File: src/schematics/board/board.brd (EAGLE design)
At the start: 50.8 x 35.6 mm, 26 parts, among them P1 PN61729-S, Q1 12MHz, U1 MCP17003302E/TO, U2 PIC18LF14K50-E-P

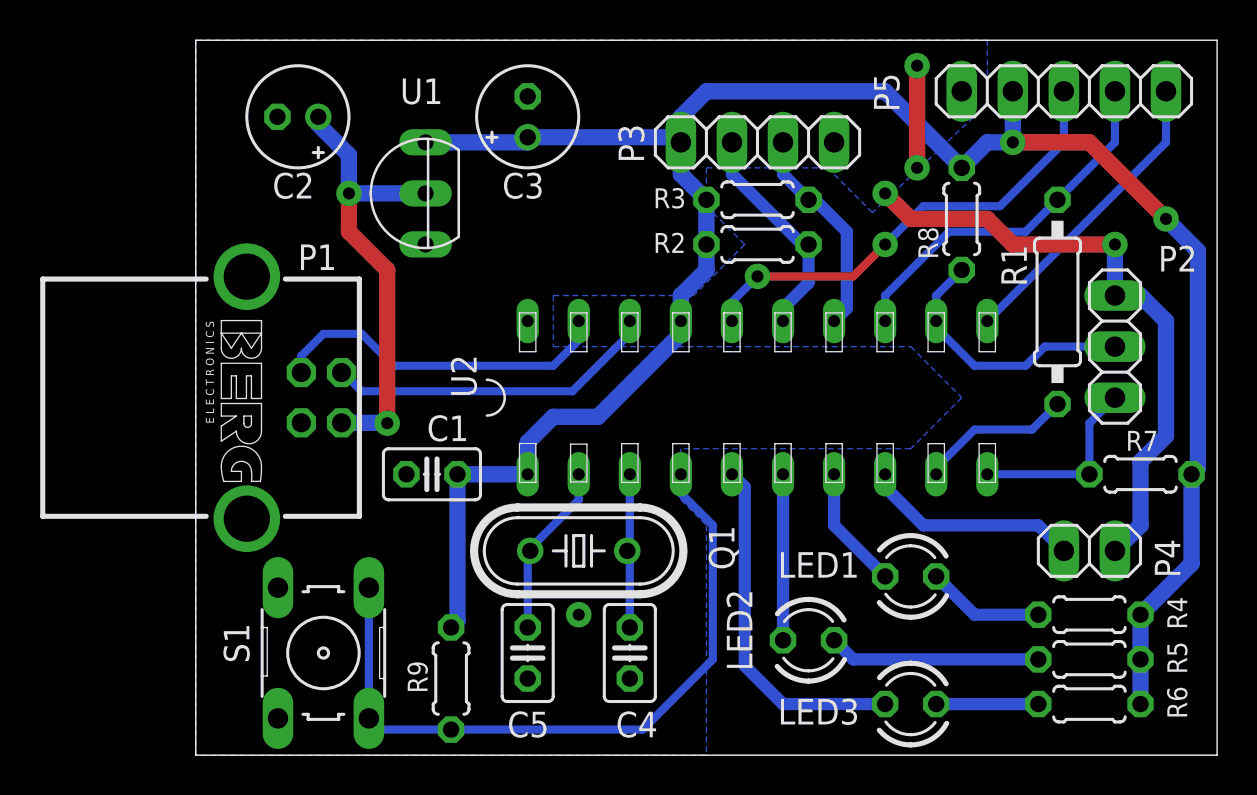
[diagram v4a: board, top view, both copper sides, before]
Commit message: Fixed PCB libraries
Some components in the extended Microxhip library had wrong dual-in-line
package drawings.

The libraries were renamed as "local" instead of "extended".

Minor fixes in both schematics and PCBs.

Andrea Zoppi
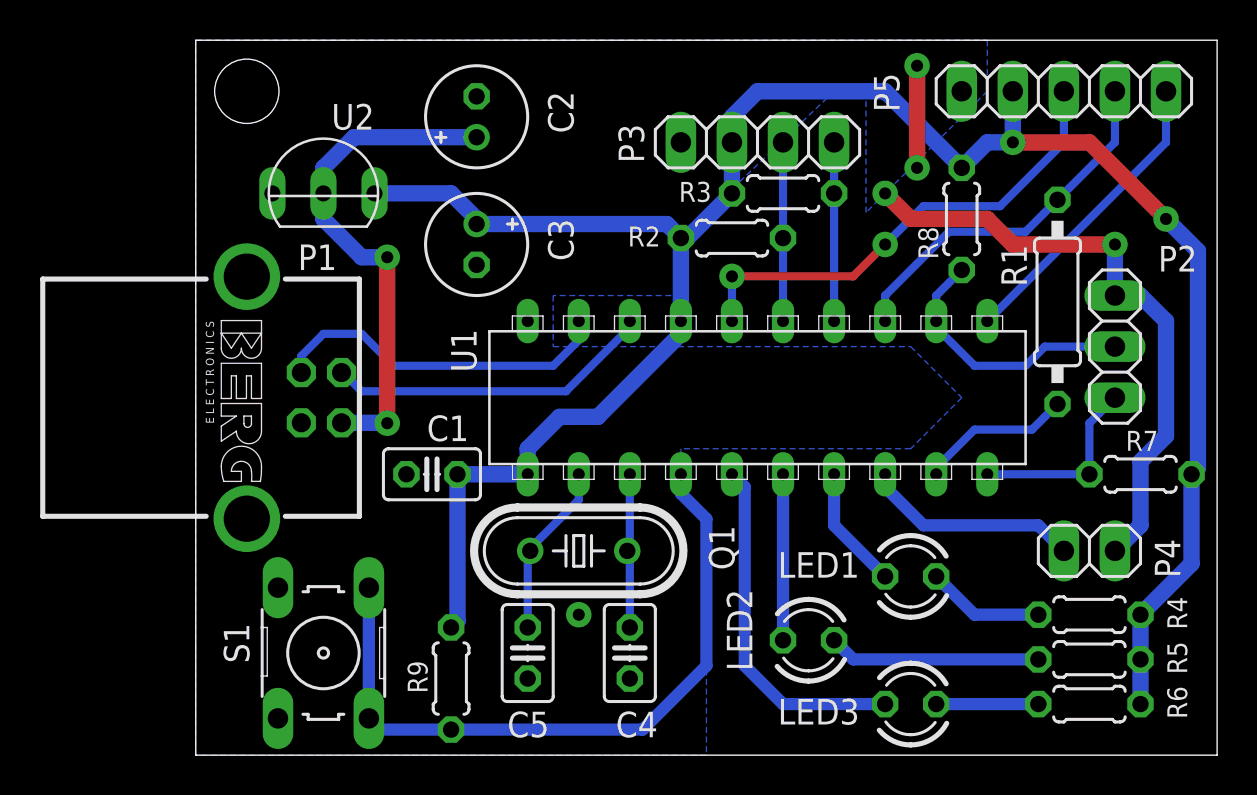
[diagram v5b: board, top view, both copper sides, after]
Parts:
- U1: value MCP17003302E/TO -> PIC18F14K50-E-P; device microchip_extended:TO-92 -> microchip_local:DIP-20
- U2: value PIC18LF14K50-E-P -> MCP17003302E/TO; device microchip_extended:PIC18F14K50-E/P -> microchip_local:TO-92
- moved U2 22.7 mm to (6.35, 27.9), turned to 0 degrees
- moved U1 19.4 mm to (27.9, 17.8)
- moved C2 8.89 mm to (14.0, 31.8), turned to 90 degrees
- moved C3 6.84 mm to (14.0, 25.4), turned to 270 degrees
- moved R2 1.31 mm to (26.7, 25.7)
- moved R3 1.31 mm to (29.2, 27.9)
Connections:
- removed net ENC_A: P3.2, R2.1, U2.15
- removed net ENC_B: P3.3, R3.1, U2.14
- new net QA: P3.3, R2.1, U1.15
- new net QB: P3.4, R3.1, U1.14
- net +3V3: now also P3.2, U1.1, U1.17, U2.OUT; no longer P3.1, U1.OUT, U2.1, U2.17
- net +5V: now also U2.IN; no longer U1.IN
- net AUXIN: now also U1.8; no longer U2.8
- net D+: now also U1.19; no longer U2.19
- net D-: now also U1.18; no longer U2.18
- net GND: now also P3.1, U1.20, U2.GND; no longer P3.4, U1.GND, U2.20
- net GREEN: now also U1.7; no longer U2.7
- net MOSI: now also U1.9; no longer U2.9
- net MOTION: now also U1.16; no longer U2.16
- net N$2: now also U1.3; no longer U2.3
- net N$3: now also U1.2; no longer U2.2
- net RED: now also U1.5; no longer U2.5
- net RST: now also U1.4; no longer U2.4
- net RX: now also U1.12; no longer U2.12
- net SCLK: now also U1.11; no longer U2.11
- net SDIO: now also U1.13; no longer U2.13
- net TX: now also U1.10; no longer U2.10
- net YELLOW: now also U1.6; no longer U2.6
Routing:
- net ENC_A: track 11.2 -> 0.00 mm
- net ENC_B: track 10.7 -> 0.00 mm
- net QB: track 0.00 -> 8.89 mm
- net QA: track 0.00 -> 8.89 mm
- net +5V: track 22.8 -> 25.3 mm
- net +3V3: track 104.4 -> 105.2 mm
- net MOTION: track 23.3 -> 24.0 mm

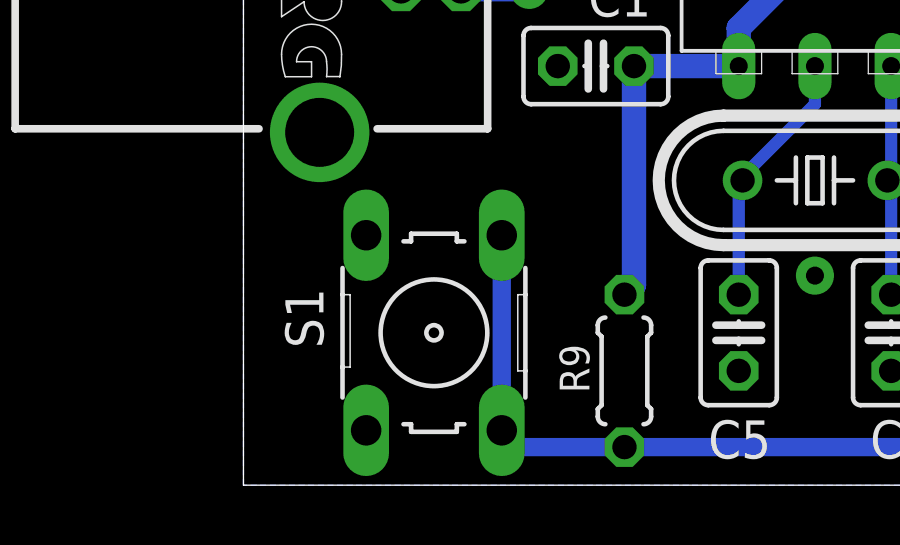
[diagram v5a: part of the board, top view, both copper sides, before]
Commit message: WIP: Improving debug messages
The debug console is being improved to reduce the footprint (by using
preprocessor definitions) and the overall performance.

Andrea Zoppi
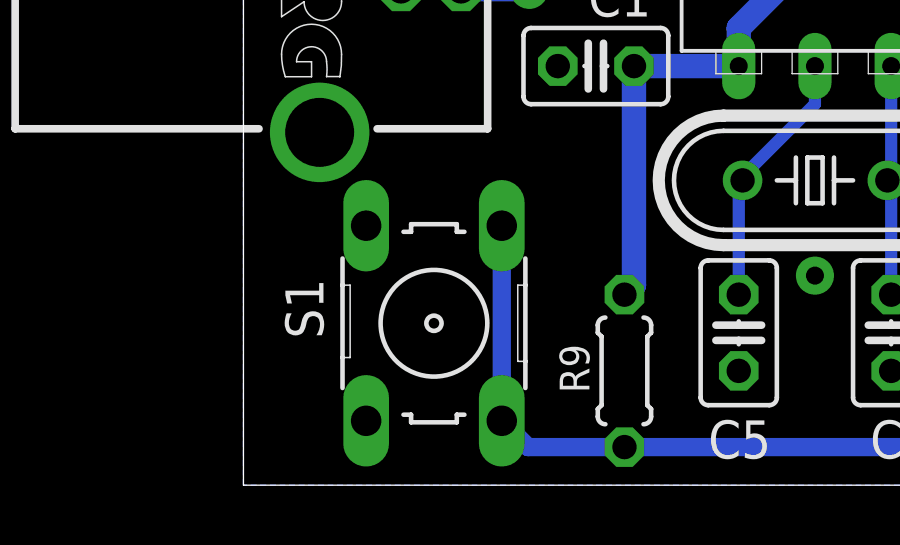
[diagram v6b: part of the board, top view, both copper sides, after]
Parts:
- U1: device microchip_local:DIP-20 -> microchip_local:DIL20
- moved S1 0.32 mm to (6.35, 5.40)
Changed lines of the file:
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@@
 <attribute name="NAME" x="25.527" y="11.43" size="1.27" layer="25" ratio="10" rot="R270"/>
 </element>
-<element name="S1" library="switch-omron" package="B3F-10XX" value="" x="6.35" y="5.08" smashed="yes" rot="R270">
-<attribute name="OC_NEWARK" value="36M3542" x="-26.67" y="-13.97" size="1.778" layer="27" rot="R270" display="off"/>
-<attribute name="MPN" value="B3F-1000" x="-26.67" y="-13.97" size="1.778" layer="27" rot="R270" display="off"/>
-<attribute name="MF" value="" x="-26.67" y="-13.97" size="1.778" layer="27" rot="R270" display="off"/>
-<attribute name="OC_FARNELL" value="176432" x="-26.67" y="-13.97" size="1.778" layer="27" rot="R270" display="off"/>
-<attribute name="NAME" x="2.667" y="4.572" size="1.27" layer="25" ratio="10" rot="R90"/>
-<attribute name="VALUE" x="1.27" y="8.128" size="1.27" layer="27" ratio="10" rot="R270"/>
+<element name="S1" library="switch-omron" package="B3F-10XX" value="" x="6.35" y="5.3975" smashed="yes" rot="R270">
+<attribute name="OC_NEWARK" value="36M3542" x="-26.67" y="-13.6525" size="1.778" layer="27" rot="R270" display="off"/>
+<attribute name="MPN" value="B3F-1000" x="-26.67" y="-13.6525" size="1.778" layer="27" rot="R270" display="off"/>
+<attribute name="MF" value="" x="-26.67" y="-13.6525" size="1.778" layer="27" rot="R270" display="off"/>
+<attribute name="OC_FARNELL" value="176432" x="-26.67" y="-13.6525" size="1.778" layer="27" rot="R270" display="off"/>
+<attribute name="NAME" x="2.667" y="4.8895" size="1.27" layer="25" ratio="10" rot="R90"/>
+<attribute name="VALUE" x="1.27" y="8.4455" size="1.27" layer="27" ratio="10" rot="R270"/>
 </element>
 <element name="P2" library="pinhead" package="1X03" value="" x="45.72" y="20.32" smashed="yes" rot="R90">
@@
 <attribute name="NAME" x="11.5316" y="3.0734" size="0.9906" layer="25" ratio="10" rot="R90"/>
 </element>
-<element name="U1" library="microchip_local" package="DIP-20" value="PIC18F14K50-E-P" x="27.94" y="17.78" smashed="yes" rot="R90">
+<element name="U1" library="microchip_local" package="DIL20" value="PIC18F14K50-E-P" x="27.94" y="17.78" smashed="yes" rot="R90">
 <attribute name="NAME" x="13.97" y="19.05" size="1.27" layer="25" rot="R90"/>
 </element>
@@
 <contactref element="U1" pad="4"/>
 <wire x1="24.13" y1="13.0175" x2="24.13" y2="13.97" width="0.6096" layer="16"/>
-<wire x1="8.6106" y1="1.8288" x2="8.6106" y2="8.3312" width="0.6096" layer="16"/>
-<wire x1="8.6106" y1="1.8288" x2="9.1694" y2="1.27" width="0.6096" layer="16"/>
-<wire x1="9.1694" y1="1.27" x2="12.7" y2="1.27" width="0.6096" layer="16"/>
+<wire x1="8.6106" y1="2.1463" x2="8.6106" y2="8.6487" width="0.6096" layer="16"/>
+<wire x1="8.6106" y1="2.1463" x2="9.4869" y2="1.27" width="0.6096" layer="16"/>
+<wire x1="9.4869" y1="1.27" x2="12.7" y2="1.27" width="0.6096" layer="16"/>
 </signal>
 <signal name="TX">
